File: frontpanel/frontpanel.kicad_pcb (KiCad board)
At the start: 2 copper layers, 103 x 30.5 mm, 14 parts

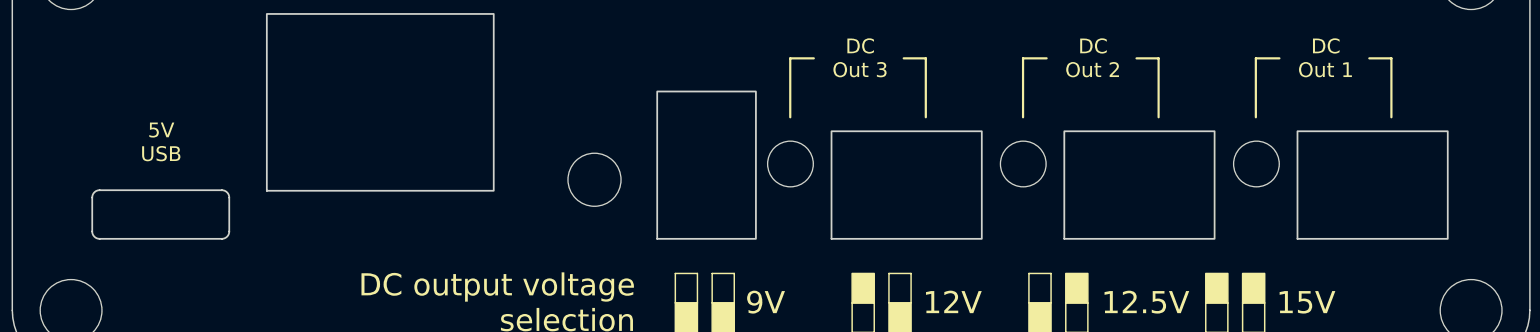
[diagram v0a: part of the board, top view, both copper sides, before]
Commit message: Add backpanel
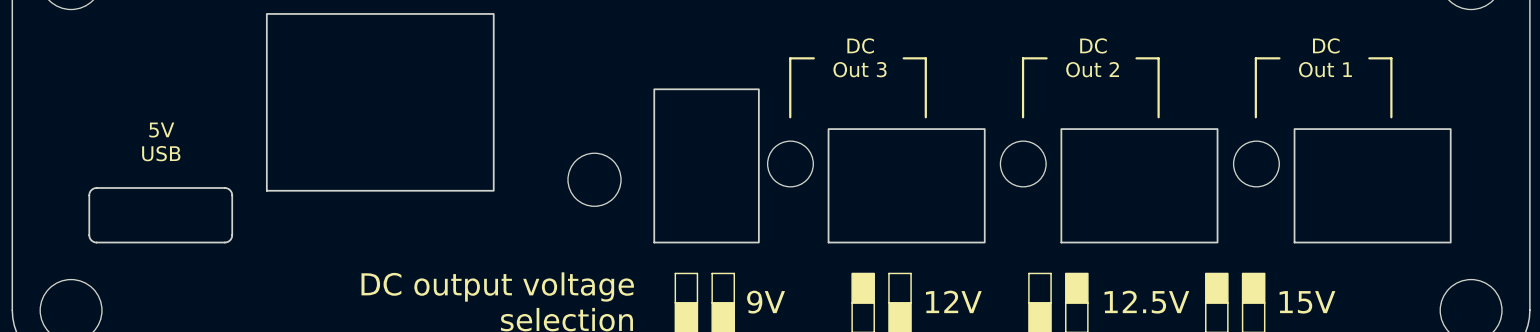
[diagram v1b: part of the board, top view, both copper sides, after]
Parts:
- moved REF** 0.25 mm to (60.1, 71.9)
- moved REF** 0.25 mm to (126.7, 71.9)
- moved REF** 0.25 mm to (98.4, 71.9)
- moved REF** 0.25 mm to (110.9, 71.9)
- moved REF** 0.25 mm to (142.5, 71.9)
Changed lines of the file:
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@@
   (net 0 "")
   (footprint "Frontpanel:USB-C_C167321" (layer "F.Cu")
-    (at 60.075 71.65)
+    (at 60.075 71.9)
     (fp_text reference "REF**" (at 0 1.85 unlocked) (layer "F.SilkS") hide
       (effects (font (size 1 1) (thickness 0.15)))
@@
     )
     (fp_rect (start -4.65 0) (end 4.45 -3.2) (layer "Eco1.User") (width 0.01) (fill none))
-    (fp_line (start 4.65 -2.8) (end 4.65 -0.5) (layer "Edge.Cuts") (width 0.12))
-    (fp_line (start 4.15 0) (end -4.15 0) (layer "Edge.Cuts") (width 0.12))
-    (fp_line (start -4.65 -0.5) (end -4.649999 -2.800001) (layer "Edge.Cuts") (width 0.12))
-    (fp_line (start -4.15 -3.3) (end 4.150001 -3.299999) (layer "Edge.Cuts") (width 0.12))
-    (fp_arc (start -4.150001 -0.000001) (mid -4.503554 -0.146447) (end -4.65 -0.5) (layer "Edge.Cuts") (width 0.12))
-    (fp_arc (start 4.150001 -3.299999) (mid 4.503553 -3.153552) (end 4.65 -2.8) (layer "Edge.Cuts") (width 0.12))
-    (fp_arc (start 4.649999 -0.499999) (mid 4.503552 -0.146447) (end 4.15 0) (layer "Edge.Cuts") (width 0.12))
-    (fp_arc (start -4.649999 -2.800001) (mid -4.503553 -3.153554) (end -4.15 -3.3) (layer "Edge.Cuts") (width 0.12))
+    (fp_line (start -4.85 -0.5) (end -4.849999 -3.200001) (layer "Edge.Cuts") (width 0.12))
+    (fp_line (start 4.85 -3.2) (end 4.85 -0.5) (layer "Edge.Cuts") (width 0.12))
+    (fp_line (start -4.35 -3.7) (end 4.350001 -3.699999) (layer "Edge.Cuts") (width 0.12))
+    (fp_line (start 4.35 0) (end -4.350001 -0.000001) (layer "Edge.Cuts") (width 0.12))
+    (fp_arc (start 4.350001 -3.699999) (mid 4.703553 -3.553552) (end 4.85 -3.2) (layer "Edge.Cuts") (width 0.12))
+    (fp_arc (start -4.849999 -3.200001) (mid -4.703553 -3.553554) (end -4.35 -3.7) (layer "Edge.Cuts") (width 0.12))
+    (fp_arc (start 4.849999 -0.499999) (mid 4.703552 -0.146447) (end 4.35 0) (layer "Edge.Cuts") (width 0.12))
+    (fp_arc (start -4.350001 -0.000001) (mid -4.703554 -0.146447) (end -4.85 -0.5) (layer "Edge.Cuts") (width 0.12))
   )
   (footprint "" (layer "F.Cu")
@@
   )
   (footprint "Frontpanel:DipSwitch_C692490" (layer "F.Cu")
-    (at 98.389505 71.65)
+    (at 98.389505 71.9)
     (fp_text reference "REF**" (at 0 -0.5 unlocked) (layer "F.SilkS") hide
       (effects (font (size 1 1) (thickness 0.15)))
@@
     )
     (fp_line (start 0 0) (end 0 -4) (layer "Eco1.User") (width 0.05))
-    (fp_rect (start -4.62 0) (end 2.08 -10) (layer "Edge.Cuts") (width 0.12) (fill none))
+    (fp_rect (start -4.82 0) (end 2.28 -10.4) (layer "Edge.Cuts") (width 0.12) (fill none))
   )
   (footprint "Frontpanel:Display_OLED_C2890608" (layer "F.Cu")
@@
     )
     (fp_line (start 0 0) (end 0 -8) (layer "Eco1.User") (width 0.05))
+    (fp_rect (start -6.75 -5.55) (end 6.75 -15.55) (layer "Eco1.User") (width 0.05) (fill none))
     (fp_rect (start -8.75 -3.3) (end 8.75 -17.8) (layer "Eco1.User") (width 0.05) (fill none))
-    (fp_rect (start -6.75 -5.55) (end 6.75 -15.55) (layer "Eco1.User") (width 0.05) (fill none))
     (fp_rect (start -9.25 -18.1) (end 9.25 0) (layer "Eco2.User") (width 0.05) (fill none))
     (fp_rect (start -7.7 -4.55) (end 7.7 -16.55) (layer "Edge.Cuts") (width 0.12) (fill none))
@@
   )
   (footprint "Frontpanel:BarrelJack_C397334" (layer "F.Cu")
-    (at 110.9 71.65)
+    (at 110.9 71.9)
     (fp_text reference "REF**" (at 0 -0.5 unlocked) (layer "F.SilkS") hide
       (effects (font (size 1 1) (thickness 0.15)))
@@
       (effects (font (size 1 1) (thickness 0.15)))
     )
+    (fp_line (start 2.05 -3.5) (end 0.05 -3.5) (layer "Eco1.User") (width 0.05))
+    (fp_line (start 1.05 -2.45) (end 1.05 -4.45) (layer "Eco1.User") (width 0.05))
     (fp_line (start 0 0) (end 0 -4) (layer "Eco1.User") (width 0.05))
-    (fp_line (start 1.05 -2.45) (end 1.05 -4.45) (layer "Eco1.User") (width 0.05))
-    (fp_line (start 2.05 -3.5) (end 0.05 -3.5) (layer "Eco1.User") (width 0.05))
-    (fp_rect (start -5.3 0) (end 4.9 -7.3) (layer "Edge.Cuts") (width 0.12) (fill none))
+    (fp_rect (start -5.5 0) (end 5.1 -7.7) (layer "Edge.Cuts") (width 0.12) (fill none))
   )
   (footprint "Frontpanel:Button_C266183" (layer "F.Cu")
@@
   )
   (footprint "Frontpanel:BarrelJack_C397334" (layer "F.Cu")
-    (at 142.525 71.65)
+    (at 142.525 71.9)
     (fp_text reference "REF**" (at 0 -0.5 unlocked) (layer "F.SilkS") hide
       (effects (font (size 1 1) (thickness 0.15)))
@@
       (effects (font (size 1 1) (thickness 0.15)))
     )
-    (fp_line (start 0 0) (end 0 -4) (layer "Eco1.User") (width 0.05))
     (fp_line (start 1.05 -2.45) (end 1.05 -4.45) (layer "Eco1.User") (width 0.05))
     (fp_line (start 2.05 -3.5) (end 0.05 -3.5) (layer "Eco1.User") (width 0.05))
-    (fp_rect (start -5.3 0) (end 4.9 -7.3) (layer "Edge.Cuts") (width 0.12) (fill none))
+    (fp_line (start 0 0) (end 0 -4) (layer "Eco1.User") (width 0.05))
+    (fp_rect (start -5.5 0) (end 5.1 -7.7) (layer "Edge.Cuts") (width 0.12) (fill none))
   )
   (footprint "Frontpanel:IndicatorLED_C417352" (layer "F.Cu")
@@
   )
   (footprint "Frontpanel:BarrelJack_C397334" (layer "F.Cu")
-    (at 126.7 71.65)
+    (at 126.7 71.9)
     (fp_text reference "REF**" (at 0 -0.5 unlocked) (layer "F.SilkS") hide
       (effects (font (size 1 1) (thickness 0.15)))
@@
       (effects (font (size 1 1) (thickness 0.15)))
     )
-    (fp_line (start 1.05 -2.45) (end 1.05 -4.45) (layer "Eco1.User") (width 0.05))
     (fp_line (start 0 0) (end 0 -4) (layer "Eco1.User") (width 0.05))
     (fp_line (start 2.05 -3.5) (end 0.05 -3.5) (layer "Eco1.User") (width 0.05))
-    (fp_rect (start -5.3 0) (end 4.9 -7.3) (layer "Edge.Cuts") (width 0.12) (fill none))
+    (fp_line (start 1.05 -2.45) (end 1.05 -4.45) (layer "Eco1.User") (width 0.05))
+    (fp_rect (start -5.5 0) (end 5.1 -7.7) (layer "Edge.Cuts") (width 0.12) (fill none))
   )
   (footprint "Frontpanel:Hole_0.165in" (layer "F.Cu")

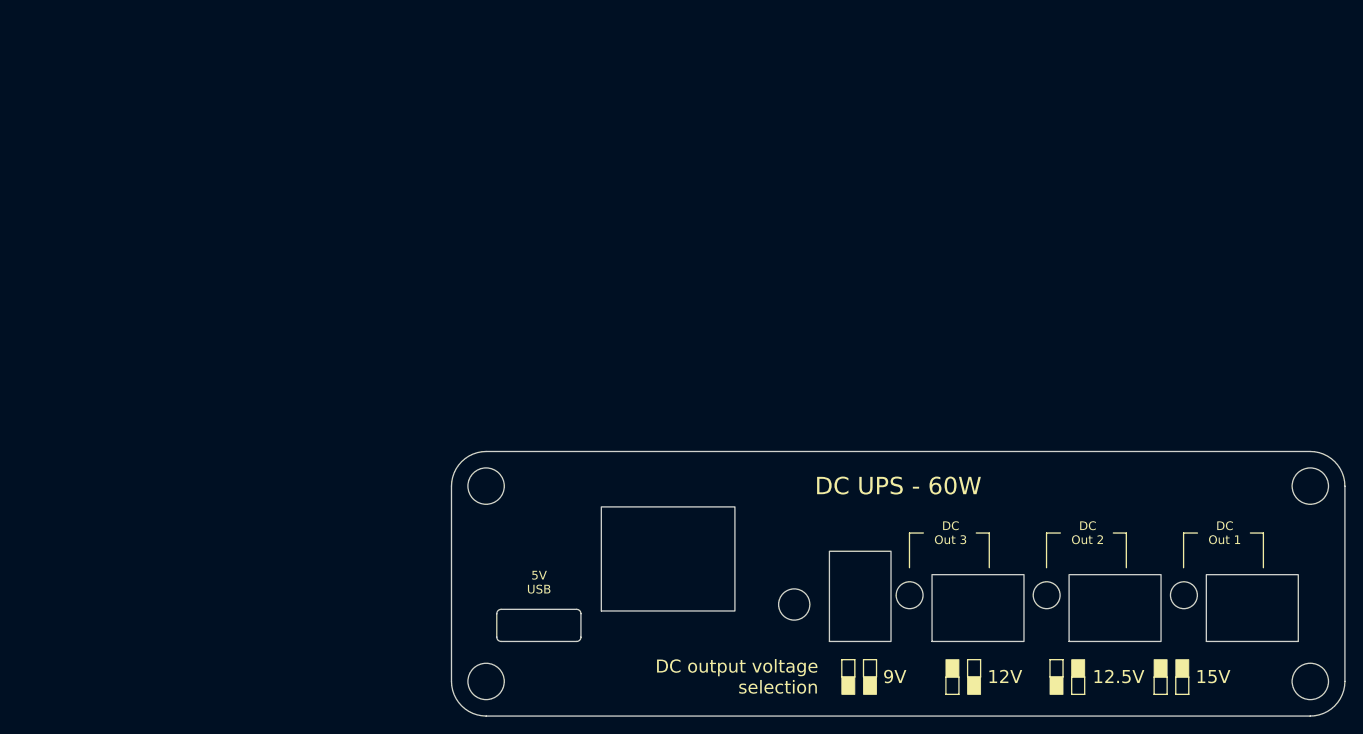
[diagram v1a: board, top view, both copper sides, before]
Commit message: Add 3d models
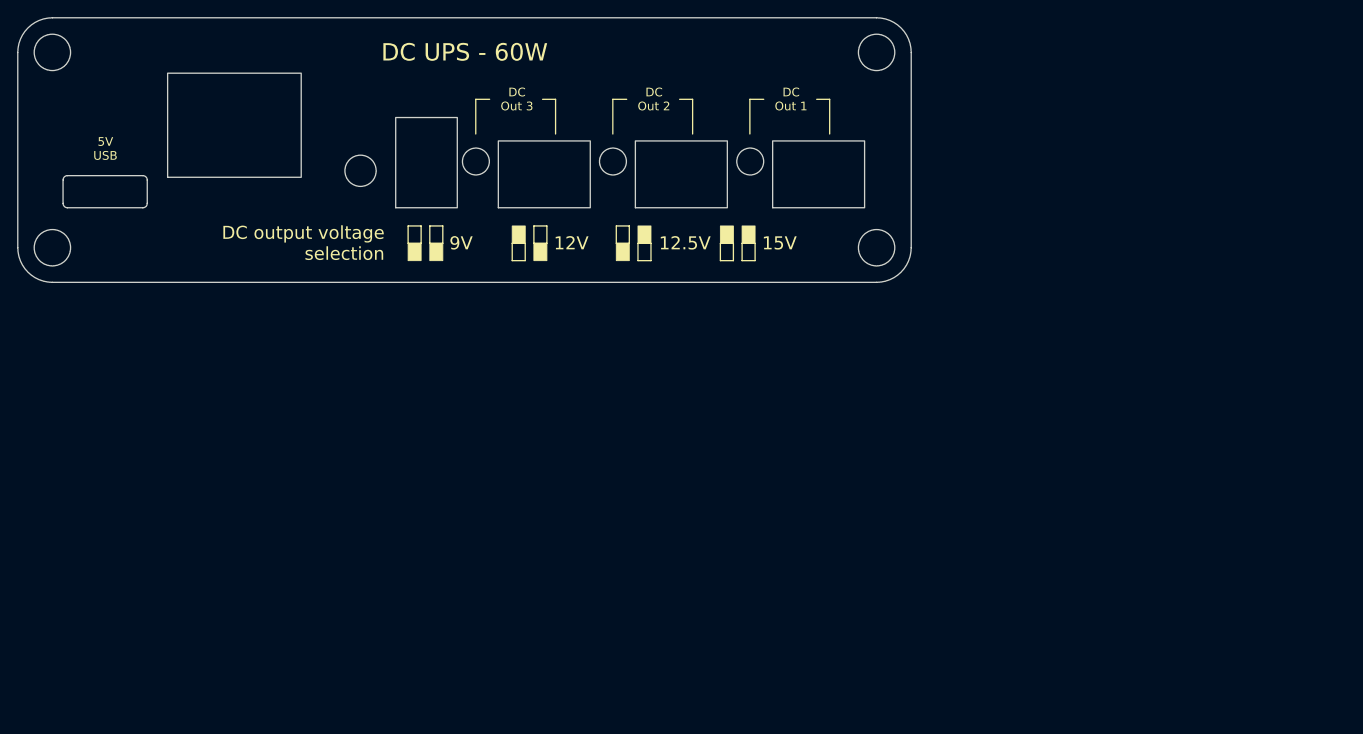
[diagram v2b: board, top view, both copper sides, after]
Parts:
- moved REF** 70.7 mm to (60.9, 21.9)
- moved REF** 70.7 mm to (10.1, 21.9)
- moved REF** 70.7 mm to (84.4, 21.6)
- moved REF** 70.7 mm to (76.7, 21.9)
- moved REF** 70.7 mm to (3.99, 3.99)
- moved REF** 70.7 mm to (48.4, 21.9)
- moved REF** 70.7 mm to (3.99, 26.5)
- moved REF** 70.7 mm to (39.5, 21.6)
- moved REF** 70.7 mm to (52.8, 21.6)
- moved REF** 70.7 mm to (92.5, 21.9)
- moved REF** 70.7 mm to (68.6, 21.6)
- moved ? 70.7 mm to (99.0, 3.99)
- moved ? 70.7 mm to (99.0, 26.5)
- moved REF** 70.7 mm to (25.0, 22.9)
